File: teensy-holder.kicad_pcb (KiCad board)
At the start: 2 copper layers, 46.5 x 56.5 mm, 30 parts, among them P1 BNC, P2 pwr, P3 input, P4 spi, P5 spi, P6 spi, P7 spi, P8 i2c, U1 Teensy3.2_DIP

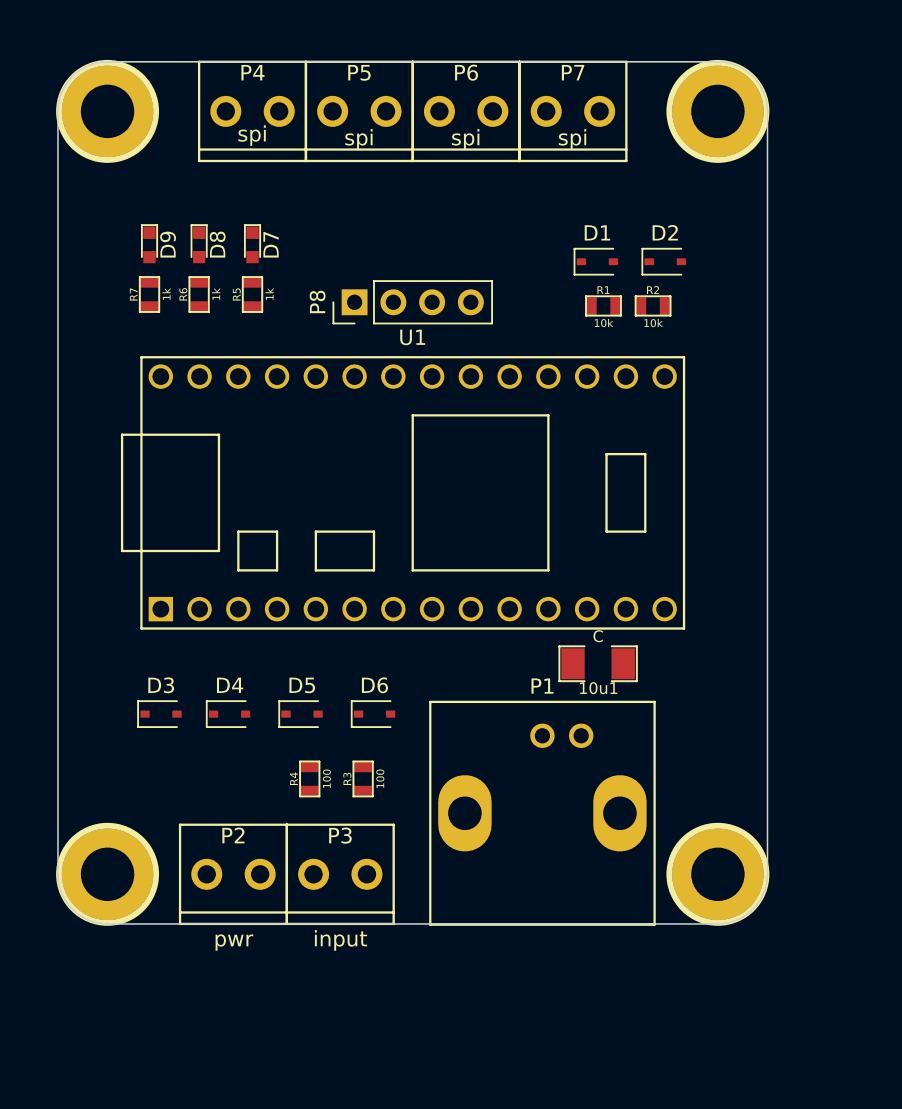
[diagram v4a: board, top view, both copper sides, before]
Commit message: Worked on routing
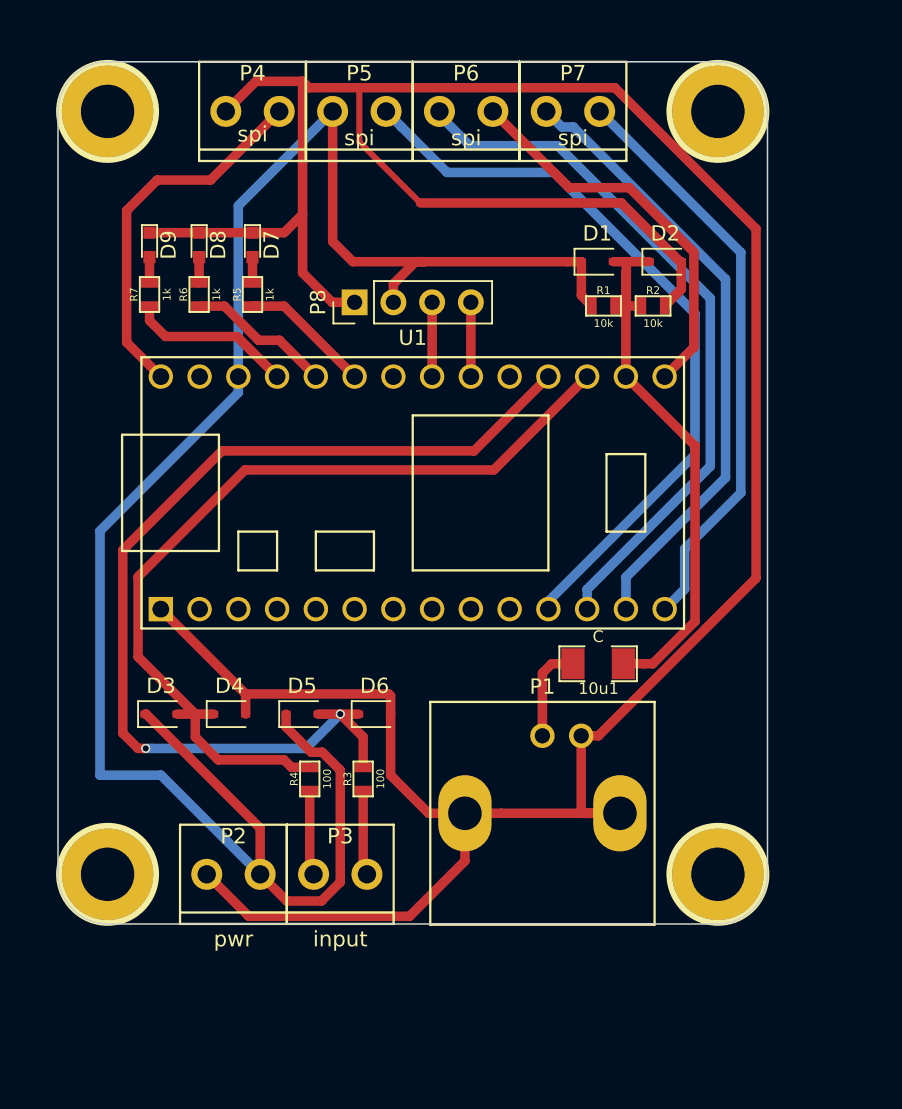
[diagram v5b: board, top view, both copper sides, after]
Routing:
- net GND: track 0.00 -> 207.0 mm
- net +3V3: track 0.00 -> 128.5 mm
- net A2: track 0.00 -> 67.0 mm, vias 0 -> 2
- net A1: track 0.00 -> 57.6 mm
- net D9: track 0.00 -> 49.1 mm
- net D10: track 0.00 -> 46.7 mm
- net MOSI: track 0.00 -> 40.6 mm
- net MISO: track 0.00 -> 38.5 mm
- net A0: track 0.00 -> 37.6 mm
- net SCK: track 0.00 -> 25.9 mm
- net VIN: track 0.00 -> 24.5 mm
- net LED3: track 0.00 -> 10.8 mm
- net LED2: track 0.00 -> 9.56 mm
- net LED1: track 0.00 -> 8.86 mm
- net Net-(10u1-Pad2): track 0.00 -> 6.36 mm
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
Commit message: Added Lables and logo
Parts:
- added G***: LOGO, visgence_parts:LOGO_BIG, B.Cu at (55.0, 65.2)
- renumbered 10u1 to 10uF
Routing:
- added copper zone on B.Cu, net GND
- added copper zone on F.Cu, net GND
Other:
- board text added: "2017 Visgence Inc."
- board text added: "3.3"
- board text added: "3.3V"
- board text added: "A0"
- board text added: "A1"
- board text added: "A2"
- board text added: "AC Coupled"
- board text added: "D11"
- board text added: "D12"
- board text added: "D13"
- board text added: "D8"
- board text added: "D9"
- board text added: "GND"
- board text added: "MISO"
- board text added: "MOSI"
- board text added: "SCK"
- board text added: "SCL"
- board text added: "SDA"
- board text added: "Teensy 3.1/3.2 Holder"
- board text added: "VIN"
